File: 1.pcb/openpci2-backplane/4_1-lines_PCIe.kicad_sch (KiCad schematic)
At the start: 24 parts, among them J10 10018784-10210TLF, J11 10018784-10210TLF, J12 10018784-10210TLF, J5 1-2199230-6, J6 1-2199230-6, J7 10018784-10210TLF, J8 1-2199230-6, J9 1-2199230-6

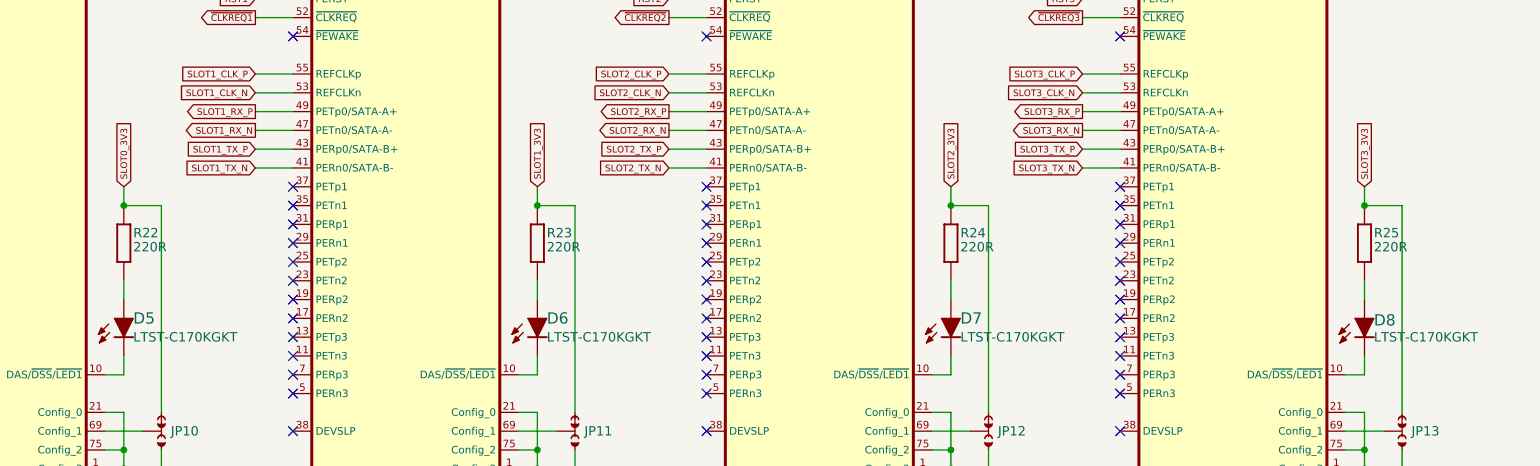
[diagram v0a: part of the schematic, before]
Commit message: Replaced Clock generator
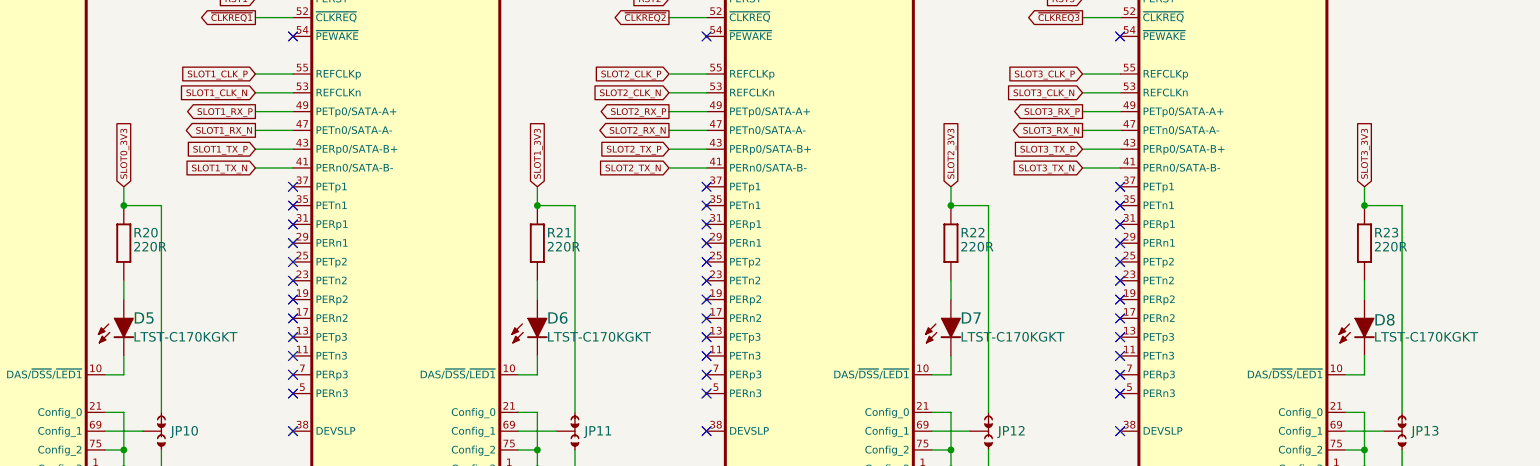
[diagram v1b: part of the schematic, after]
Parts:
- C62, C63, C64, C65: DigiKey 399-3683-1-ND -> PCE4579CT-ND; Mouser 80-T491A106K0067280 -> 667-EEE-1CA101WAP; TME T491A106K006AT -> EEE1CA101WAP
- JP10, JP11, JP12, JP13: value ~ -> n/a
- renumbered R22 to R20, R23 to R21, R24 to R22, R25 to R23

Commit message: Schematics update
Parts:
- renumbered C62 to C65, C63 to C66, C64 to C67, C65 to C68
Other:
- note added: "Add four +3.3V powers stepdown converters for this section!"

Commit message: PCIe connectors update
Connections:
- net SLOT0_RX_N: no longer J7.B15 (PETn0)
- net SLOT0_RX_P: no longer J7.B14 (PETp0)
- net SLOT0_TX_N: no longer J7.A17 (PERn0)
- net SLOT0_TX_P: no longer J7.A16 (PERp0)
- net SLOT1_RX_N: no longer J10.B15 (PETn0)
- net SLOT1_RX_P: no longer J10.B14 (PETp0)
- net SLOT1_TX_N: no longer J10.A17 (PERn0)
- net SLOT1_TX_P: no longer J10.A16 (PERp0)
- net SLOT2_RX_N: no longer J11.B15 (PETn0)
- net SLOT2_RX_P: no longer J11.B14 (PETp0)
- net SLOT2_TX_N: no longer J11.A17 (PERn0)
- net SLOT2_TX_P: no longer J11.A16 (PERp0)
- net SLOT3_RX_N: no longer J12.B15 (PETn0)
- net SLOT3_RX_P: no longer J12.B14 (PETp0)
- net SLOT3_TX_N: no longer J12.A17 (PERn0)
- net SLOT3_TX_P: no longer J12.A16 (PERp0)
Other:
- note added: "Connect to CLKREQ?"
- moved on the sheet: C65, C66, C67, C68
